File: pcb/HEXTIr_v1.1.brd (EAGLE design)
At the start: 71.1 x 38.1 mm, 28 parts, among them CN1 HEX-BUS, IC1 ATMEGA328

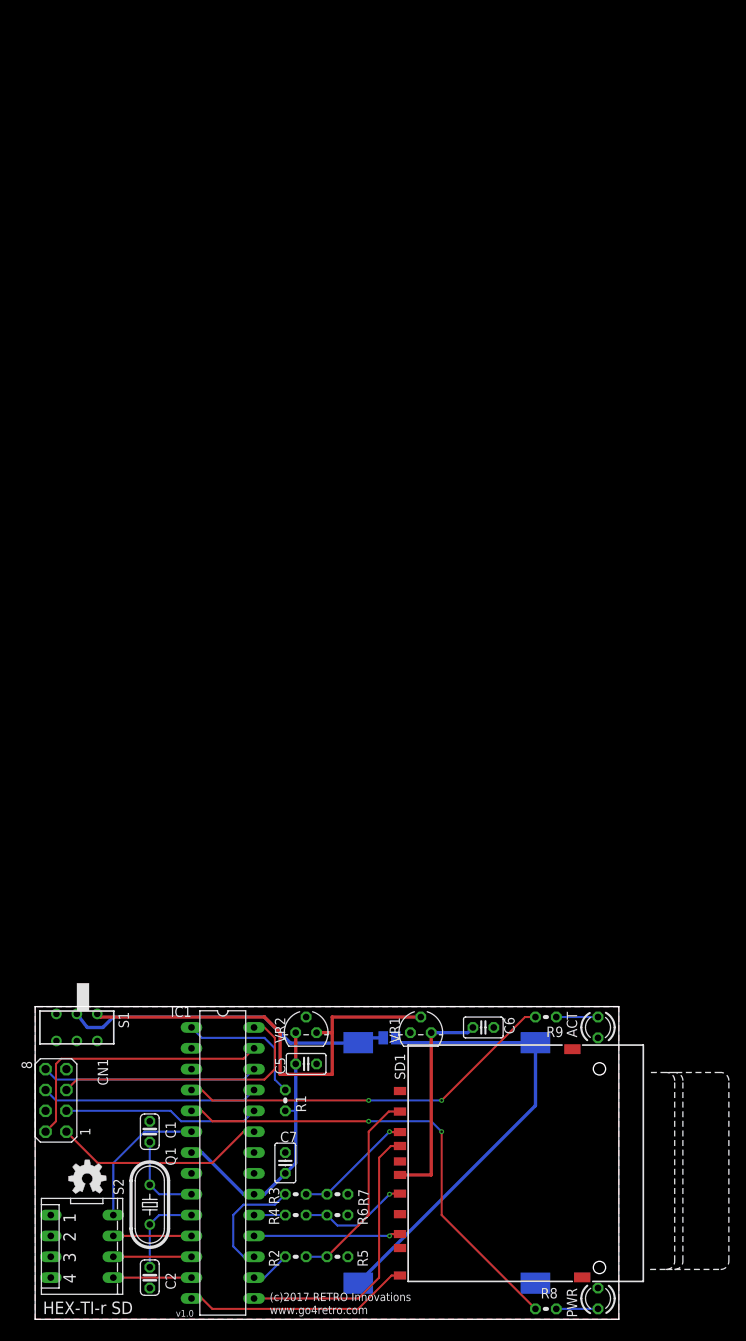
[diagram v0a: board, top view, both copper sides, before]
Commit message: Create Arduino-compatible PCB layout
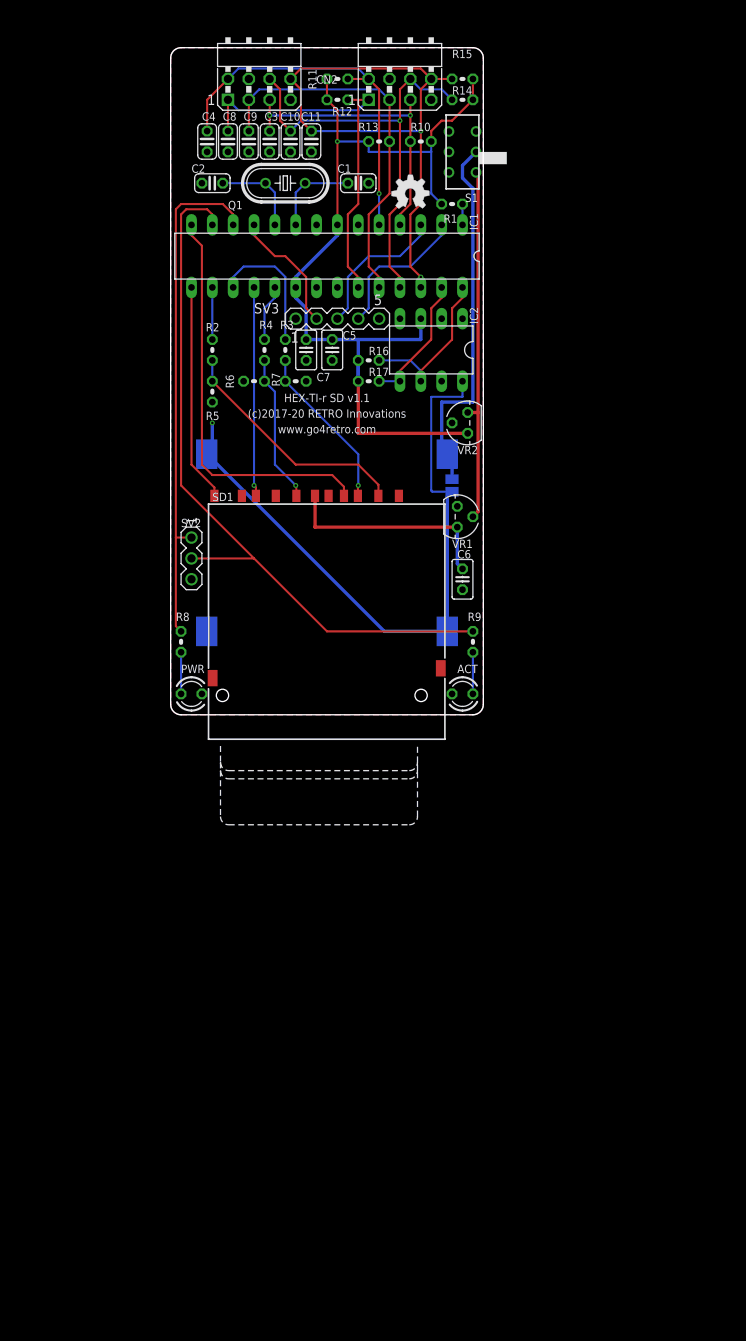
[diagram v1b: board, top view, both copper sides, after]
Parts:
- removed CN1: HEX-BUS, ti_cc40:HEX-BUS
- removed S2: (no value), switch-dil:DP-04
- added C10, C11, C3, C4, C8, C9: (no value), rcl:C025-024X044
- added CN2: HEX-BUS_DUAL, ti-cc40:HEX-BUS_DUAL
- added IC2: DS1307, dallas-rtc:DIL08
- added R10, R11, R12, R13, R14, R15: 8K2, rcl:0204V
- added R16, R17: 4K7, rcl:0204V
- added SV2: (no value), con-lstb-rp:MA03-1
- added SV3: (no value), con-lstb-rp:MA05-1
- Q1: value (none) -> 16MHz
- S1: value OFF-ON -> ON
- VR1: value MCP1700-3302 -> MCP1700
- moved C2 133.6 mm to (-14.0, 64.8), turned to 180 degrees
- moved GOLD_ORB_SM1 126.3 mm to (10.2, 63.5)
- moved Q1 125.6 mm to (-5.08, 64.8), turned to 0 degrees
- moved C1 118.3 mm to (3.81, 64.8), turned to 0 degrees
- moved S1 116.6 mm to (16.5, 68.6), turned to 270 degrees
- moved IC1 111.2 mm to (0.00, 55.9), turned to 180 degrees
- moved R1 111.1 mm to (15.2, 62.2), turned to 0 degrees
- moved R2 111.0 mm to (-14.0, 44.5), turned to 270 degrees
- moved R5 106.5 mm to (-14.0, 39.4), turned to 90 degrees
- moved R4 105.5 mm to (-7.62, 44.5), turned to 270 degrees
- moved R3 102.9 mm to (-5.08, 44.5), turned to 270 degrees
- moved R6 102.1 mm to (-8.89, 40.6), turned to 0 degrees
- moved R7 99.2 mm to (-3.81, 40.6)
- moved C7 99.1 mm to (-2.54, 44.5), turned to 270 degrees
- moved R8 92.6 mm to (-17.8, 8.89), turned to 90 degrees
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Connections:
- removed net N$20: IC1.13, S2.5
- removed net N$21: IC1.12, S2.6
- removed net N$22: IC1.11, S2.7
- removed net N$24: IC1.5, R8.2
- removed net N$25: IC1.28, R9.2
- removed net N$7: ALL3V3.2, G1.+, G2.-
- new net ACT: IC1.13, R9.2, SV2.2
- new net PWR: IC1.12, R8.2, SV2.1
- new net RXD0: IC1.2, SV3.4
- new net SCL: IC1.28, IC2.6, R16.2
- new net SDA: IC1.27, IC2.5, R17.2
- new net TXD0: IC1.3, SV3.3
- new net TXD1: IC1.11, SV3.2
- new net VCC/2: ALL3V3.2, G1.+, G2.-, IC2.8
- net !HSK: now also C4.1, CN2.5, CN2.5', IC1.5, R11.2; no longer CN1.5, IC1.27
- net +5V: now also IC2.3, R10.1, R11.1, R12.1, R13.1, R14.1, R15.1, R16.1, R17.1
- net BAV: now also C3.1, CN2.3, CN2.3', R10.2; no longer CN1.3
- net D0: now also C8.1, CN2.1, CN2.1', R12.2; no longer CN1.1
- net D1: now also C9.1, CN2.2, CN2.2', R13.2; no longer CN1.2
- net D2: now also C10.1, CN2.7, CN2.7', R14.2; no longer CN1.7
- net D3: now also C11.1, CN2.8, CN2.8', R15.2; no longer CN1.8
- net GND: now also C10.2, C11.2, C3.2, C4.2, C8.2, C9.2, CN2.4, CN2.4', IC2.4, SV2.3, SV3.1, SV3.5; no longer CN1.4, S2.1, S2.2, S2.3, S2.4
- net N$23: no longer S2.8
- net N$5: now also IC1.15; no longer IC1.14
- net N$6: now also IC1.14; no longer IC1.15
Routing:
- net ACT: track 0.00 -> 89.2 mm
- net VCC/2: track 0.00 -> 79.3 mm, vias 0 -> 1
- net +5V: track 33.5 -> 110.0 mm, vias 0 -> 1
- net PWR: track 0.00 -> 62.6 mm
- net N$24: track 57.9 -> 0.00 mm, vias 2 -> 0
- net N$7: track 55.5 -> 0.00 mm
- net N$25: track 45.4 -> 0.00 mm, vias 2 -> 0
- net D3: track 26.5 -> 68.5 mm, vias 0 -> 2
- net D2: track 26.5 -> 54.4 mm, vias 0 -> 1
- net D1: track 23.9 -> 46.4 mm
- net D0: track 26.0 -> 48.5 mm
- net SCL: track 0.00 -> 20.4 mm
- net TXD0: track 0.00 -> 17.9 mm
- net RXD0: track 0.00 -> 17.9 mm
- net N$23: track 17.5 -> 0.00 mm
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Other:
- board size 71.1 x 38.1 mm -> 38.1 x 81.3 mm
- board text added: "(c)2017-20 RETRO Innovations"
- board text added: "HEX-TI-r SD v1.1"
- board text removed: "(c)2017 RETRO Innovations"
- board text removed: "HEX-TI-r SD"
- board text removed: "v1.0"

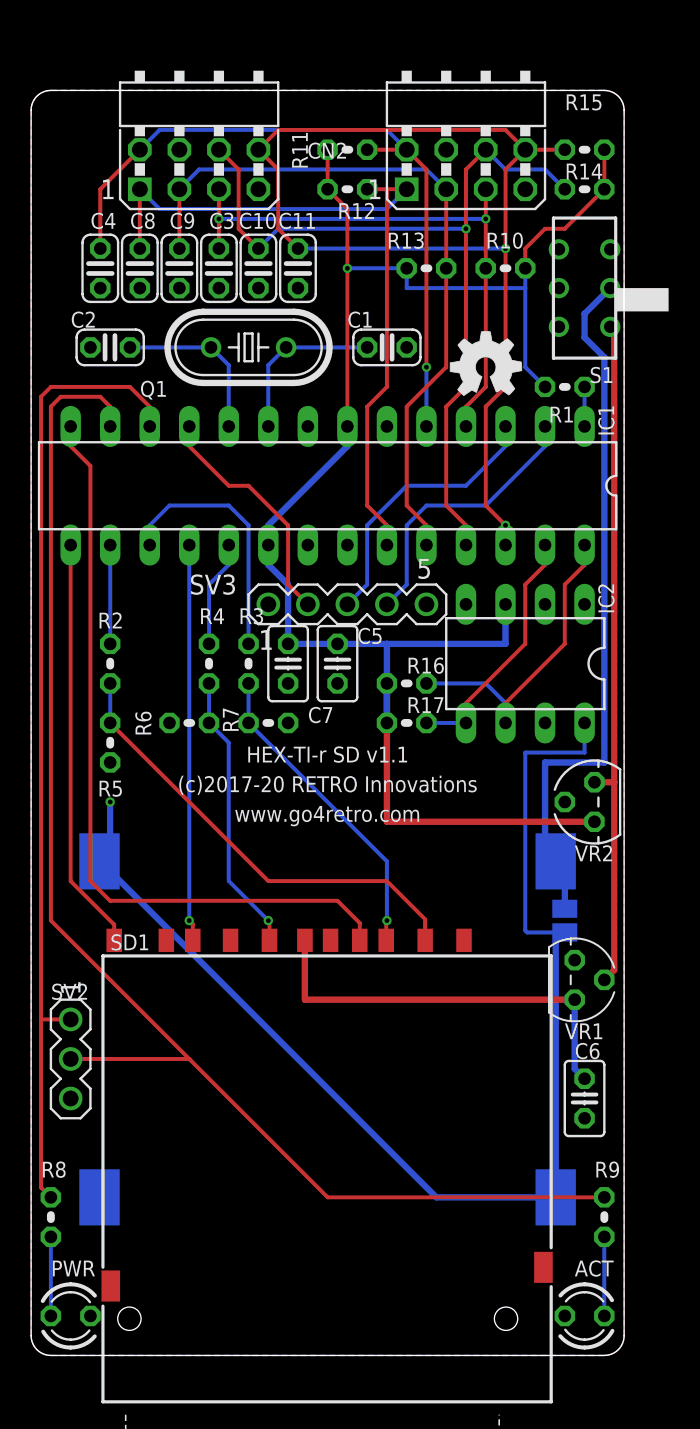
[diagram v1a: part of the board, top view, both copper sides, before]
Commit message: Clean up old unused code fragments and start reducing dependence on str*() functions.
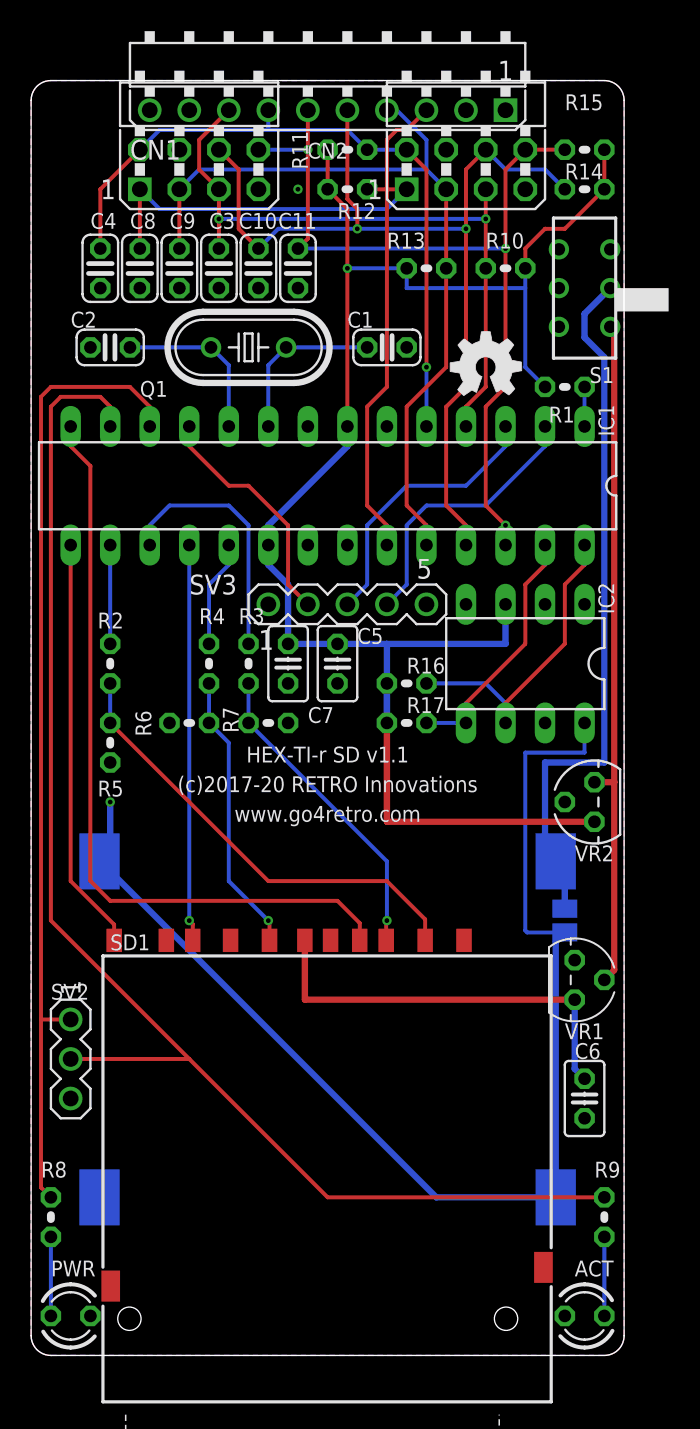
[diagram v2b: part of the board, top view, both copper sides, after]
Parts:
- added CN1: DOCK-BUSR, ti-cc40:DOCK-BUS-RP
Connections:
- new net PWN_IN: CN1.2
- new net PWR_OUT: CN1.1
- net !HSK: now also CN1.7
- net BAV: now also CN1.8
- net D0: now also CN1.3
- net D1: now also CN1.4
- net D2: now also CN1.5
- net D3: now also CN1.6
- net GND: now also CN1.10
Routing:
- net D3: track 68.5 -> 55.2 mm, vias 2 -> 3
- net D2: track 54.4 -> 62.3 mm, vias 1 -> 2
- net D0: track 48.5 -> 55.0 mm
- net BAV: track 36.7 -> 43.1 mm
- net D1: track 46.4 -> 51.7 mm
- net !HSK: track 46.4 -> 45.2 mm
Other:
- board size 38.1 x 81.3 mm -> 38.1 x 81.9 mm

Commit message: Modify pin settings for base config to PCB v1.1
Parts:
- R1: value (none) -> 10K
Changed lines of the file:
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@@
 <attribute name="VALUE" x="-12.192" y="67.437" size="1.27" layer="27" ratio="10" rot="R180"/>
 </element>
-<element name="R1" library="resistor" package="0204V" value="" x="15.24" y="62.23" smashed="yes">
+<element name="R1" library="resistor" package="0204V" value="10K" x="15.24" y="62.23" smashed="yes">
 <attribute name="NAME" x="15.875" y="60.96" size="1.016" layer="25" font="vector" ratio="10" rot="R180"/>
 <attribute name="VALUE" x="13.1064" y="59.9186" size="1.27" layer="27" ratio="10"/>
